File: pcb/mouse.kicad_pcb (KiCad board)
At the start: 2 copper layers, 70 x 45 mm, 74 parts, among them J1 USB_C_Receptacle_USB2.0, J2 Conn_01x05, J3 Conn_02x03_Counter_Clockwise, J4 Conn_01x06, J5 Conn_01x06, SW1 SW_Push_SPDT, SW2 SW_Push_SPDT, SW3 SW_Push_SPDT, SW4 SW_Push_SPDT, SW5 RotaryEncoder, SW6 SW_Push, U1 pmw3360-t2qu, U2 TLV70018_SOT23-5, U3 STM32F042K6Tx, U4 TLV70033_SOT23-5

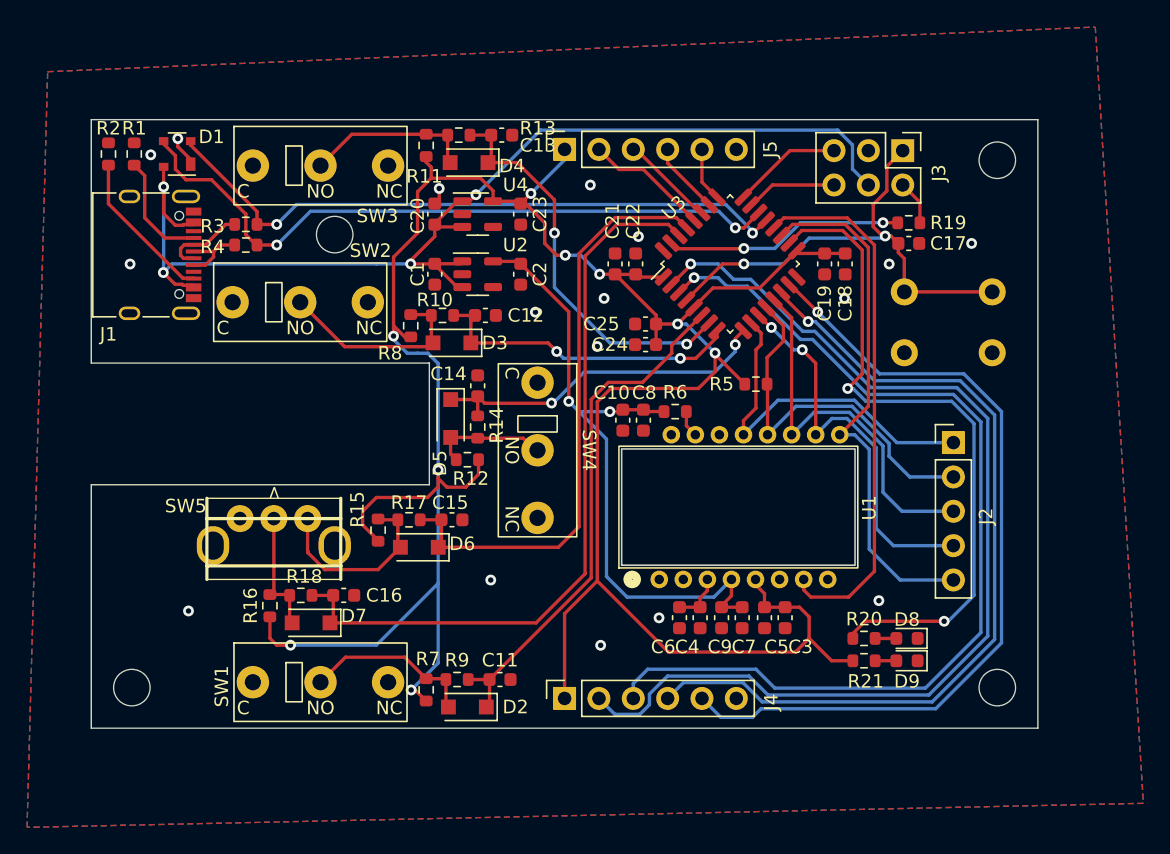
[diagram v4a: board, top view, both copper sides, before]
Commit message: added rounded corners to pcb
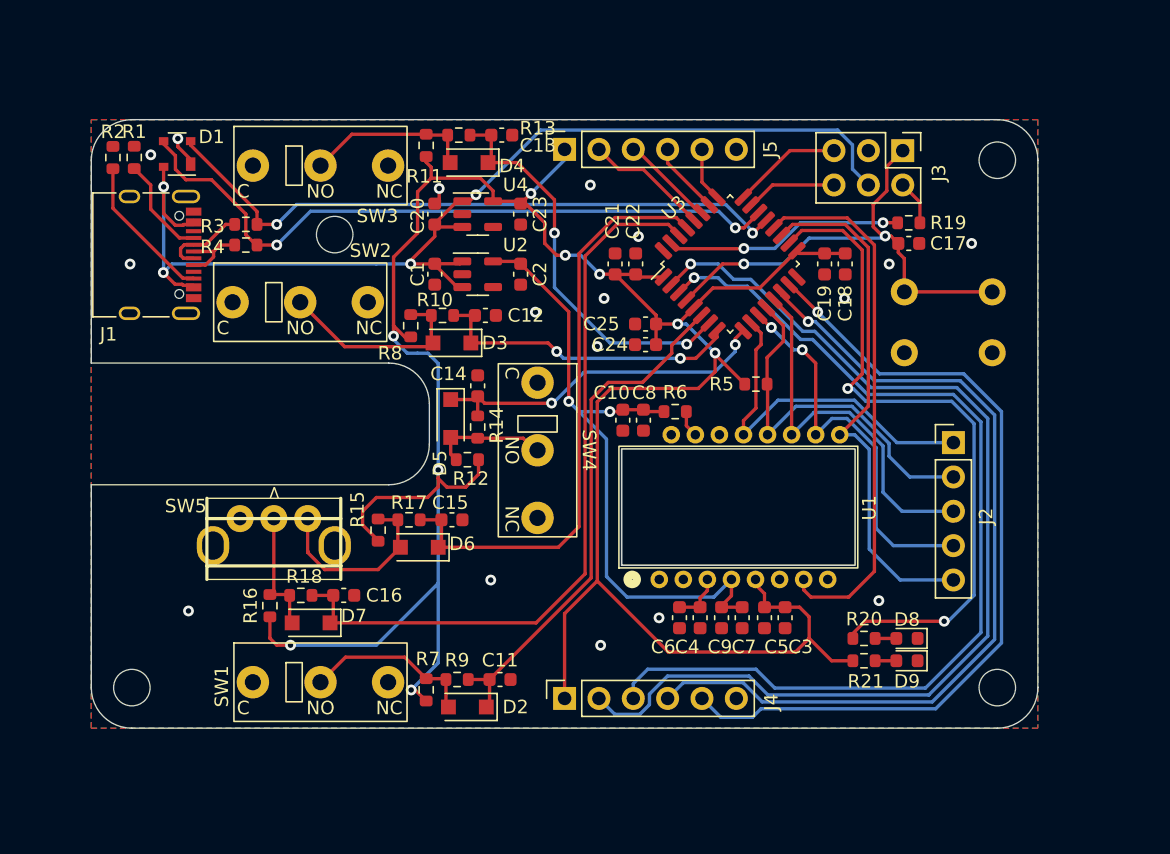
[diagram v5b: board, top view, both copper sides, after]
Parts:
- moved R2 0.42 mm to (101.6, 82.8)
- moved R1 0.25 mm to (103.2, 82.8)
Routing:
- net Net-(J1-PadA5): track 8.45 -> 7.57 mm
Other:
- outline, holes or cut-outs redrawn
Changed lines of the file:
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@@
   )
   (footprint "Resistor_SMD:R_0603_1608Metric" (layer "F.Cu")
-    (at 103.175 82.54 90)
+    (at 103.175 82.794 90)
     (descr "Resistor SMD 0603 (1608 Metric), square (rectangular) end terminal, IPC_7351 nominal, (Body size source: IPC-SM-782 page 72, https://www.pcb-3d.com/wordpress/wp-content/uploads/ipc-sm-782a_amendment_1_and_2.pdf), generated with kicad-footprint-generator")
     (tags "resistor")
@@
   )
   (footprint "Resistor_SMD:R_0603_1608Metric" (layer "F.Cu")
-    (at 101.27 82.54 90)
+    (at 101.6 82.804 90)
     (descr "Resistor SMD 0603 (1608 Metric), square (rectangular) end terminal, IPC_7351 nominal, (Body size source: IPC-SM-782 page 72, https://www.pcb-3d.com/wordpress/wp-content/uploads/ipc-sm-782a_amendment_1_and_2.pdf), generated with kicad-footprint-generator")
     (tags "resistor")
@@
     )
   )
-  (gr_line (start 125 107) (end 125 98) (layer "Edge.Cuts") (width 0.1))
-  (gr_line (start 170 80) (end 170 125) (layer "Edge.Cuts") (width 0.1))
-  (gr_line (start 100 107) (end 125 107) (layer "Edge.Cuts") (width 0.1))
-  (gr_line (start 100 80) (end 170 80) (layer "Edge.Cuts") (width 0.1))
-  (gr_line (start 100 80) (end 100 98) (layer "Edge.Cuts") (width 0.1))
-  (gr_line (start 125 98) (end 100 98) (layer "Edge.Cuts") (width 0.1))
-  (gr_line (start 100 107) (end 100 125) (layer "Edge.Cuts") (width 0.1))
-  (gr_line (start 170 125) (end 100 125) (layer "Edge.Cuts") (width 0.1))
+  (gr_line (start 125 104) (end 125 101) (layer "Edge.Cuts") (width 0.1))
+  (gr_arc (start 122 98) (mid 124.12132 98.87868) (end 125 101) (layer "Edge.Cuts") (width 0.1))
+  (gr_line (start 170 83) (end 170 122) (layer "Edge.Cuts") (width 0.1))
+  (gr_line (start 100 107) (end 122 107) (layer "Edge.Cuts") (width 0.1))
+  (gr_line (start 103 80) (end 167 80) (layer "Edge.Cuts") (width 0.1))
+  (gr_line (start 100 83) (end 100 98) (layer "Edge.Cuts") (width 0.1))
+  (gr_arc (start 170 122) (mid 169.12132 124.12132) (end 167 125) (layer "Edge.Cuts") (width 0.1))
+  (gr_arc (start 100 83) (mid 100.87868 80.87868) (end 103 80) (layer "Edge.Cuts") (width 0.1))
+  (gr_arc (start 125 104) (mid 124.12132 106.12132) (end 122 107) (layer "Edge.Cuts") (width 0.1))
+  (gr_line (start 122 98) (end 100 98) (layer "Edge.Cuts") (width 0.1))
+  (gr_arc (start 167 80) (mid 169.12132 80.87868) (end 170 83) (layer "Edge.Cuts") (width 0.1))
+  (gr_line (start 100 107) (end 100 122) (layer "Edge.Cuts") (width 0.1))
+  (gr_line (start 167 125) (end 103 125) (layer "Edge.Cuts") (width 0.1))
+  (gr_arc (start 103 125) (mid 100.87868 124.12132) (end 100 122) (layer "Edge.Cuts") (width 0.1))
   (segment (start 125.575 87.935) (end 125.4 87.76) (width 0.25) (layer "F.Cu") (net 1))
   (segment (start 105.35 84.969) (end 105.35 86.944273) (width 0.25) (layer "F.Cu") (net 1))
@@
   (segment (start 157.96875 118.364) (end 159.53125 118.364) (width 0.25) (layer "F.Cu") (net 21))
   (segment (start 157.96875 120.015) (end 159.53125 120.015) (width 0.25) (layer "F.Cu") (net 22))
-  (segment (start 105.448 88.75) (end 107.57 88.75) (width 0.25) (layer "F.Cu") (net 23))
-  (segment (start 103.175 83.365) (end 103.94952 84.13952) (width 0.25) (layer "F.Cu") (net 23))
-  (segment (start 103.94952 87.25152) (end 105.448 88.75) (width 0.25) (layer "F.Cu") (net 23))
-  (segment (start 103.94952 84.13952) (end 103.94952 87.25152) (width 0.25) (layer "F.Cu") (net 23))
+  (segment (start 104.394 84.838) (end 103.175 83.619) (width 0.25) (layer "F.Cu") (net 23))
+  (segment (start 107.57 88.75) (end 106.520009 88.75) (width 0.25) (layer "F.Cu") (net 23))
+  (segment (start 104.394 86.623991) (end 104.394 84.838) (width 0.25) (layer "F.Cu") (net 23))
+  (segment (start 106.520009 88.75) (end 104.394 86.623991) (width 0.25) (layer "F.Cu") (net 23))
   (segment (start 107.57 90.75) (end 108.444022 90.75) (width 0.25) (layer "F.Cu") (net 24))
   (segment (start 107.57 89.75) (end 109.046 89.75) (width 0.25) (layer "F.Cu") (net 24))
@@
   (segment (start 107.57 90.25) (end 106.821 90.25) (width 0.25) (layer "F.Cu") (net 25))
   (segment (start 106.821 90.25) (end 106.604 90.033) (width 0.25) (layer "F.Cu") (net 25))
-  (segment (start 107.544511 91.724511) (end 106.771511 91.724511) (width 0.25) (layer "F.Cu") (net 27))
-  (segment (start 106.771511 91.724511) (end 101.27 86.223) (width 0.25) (layer "F.Cu") (net 27))
-  (segment (start 101.27 86.223) (end 101.27 83.365) (width 0.25) (layer "F.Cu") (net 27))
-  (segment (start 107.57 91.75) (end 107.544511 91.724511) (width 0.25) (layer "F.Cu") (net 27))
+  (segment (start 101.6 86.552984) (end 106.771527 91.724511) (width 0.25) (layer "F.Cu") (net 27))
+  (segment (start 106.771527 91.724511) (end 107.544511 91.724511) (width 0.25) (layer "F.Cu") (net 27))
+  (segment (start 107.544511 91.724511) (end 107.57 91.75) (width 0.25) (layer "F.Cu") (net 27))
+  (segment (start 101.6 83.629) (end 101.6 86.552984) (width 0.25) (layer "F.Cu") (net 27))
   (segment (start 149.149 97.018) (end 149.53 96.637) (width 0.25) (layer "F.Cu") (net 29))
   (segment (start 149.53 95.782427) (end 148.781957 95.034384) (width 0.25) (layer "F.Cu") (net 29))
@@
     (polygon
       (pts
-        (xy 177.8 130.556)
-        (xy 95.25 132.334)
-        (xy 96.774 76.454)
-        (xy 174.244 73.152)
+        (xy 170 125)
+        (xy 100 125)
+        (xy 100 80)
+        (xy 170 80)
       )
     )

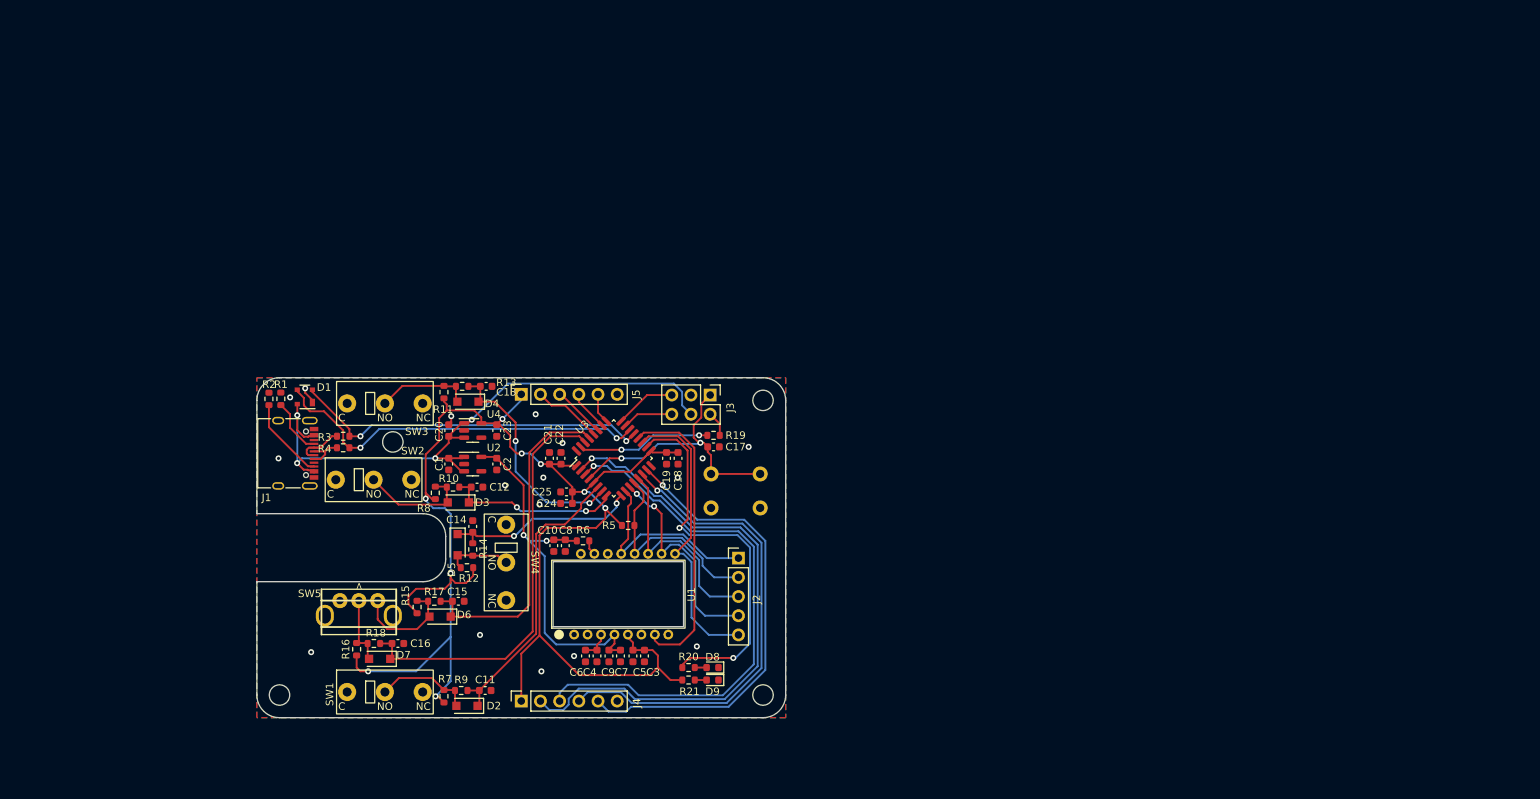
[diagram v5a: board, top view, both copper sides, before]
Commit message: manually connected GND on pcb
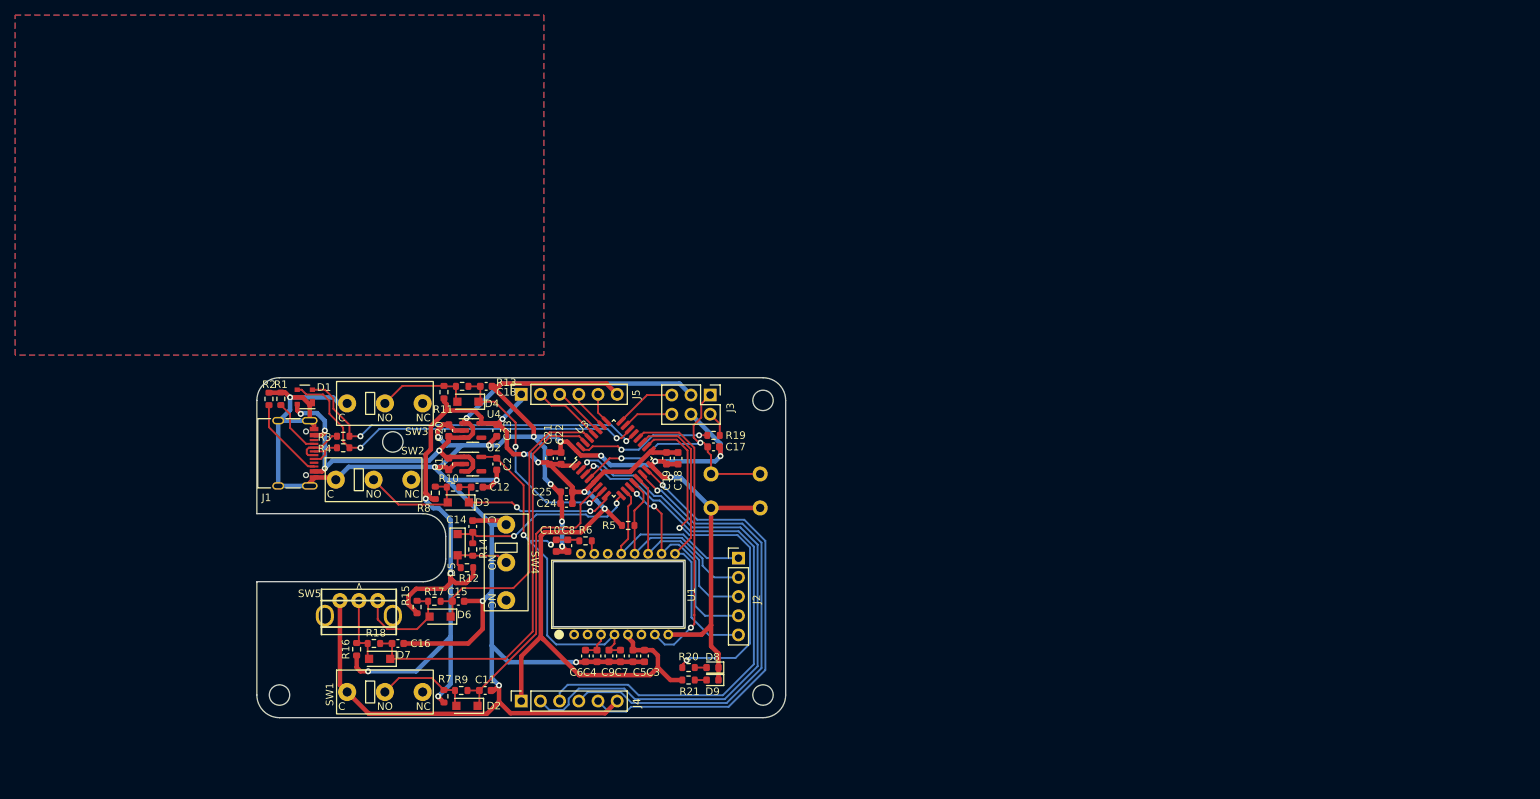
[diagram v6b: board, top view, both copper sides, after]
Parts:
- moved C10 0.33 mm to (139.6, 102.2)
- moved C8 0.33 mm to (141.2, 102.2)
- moved R6 0.33 mm to (143.5, 101.6)
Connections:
- J3 pad 3: GND -> +5V
- J3 pad 4: +5V -> GND
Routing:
- net GND: track 3.54 -> 363.6 mm
- net +5V: track 84.4 -> 79.6 mm, vias 4 -> 5
- net /buttons/ZA: track 44.3 -> 40.9 mm
- net +3V3: track 198.3 -> 196.3 mm
- net /buttons/LEFT: track 38.6 -> 39.7 mm
- net /mcu/USB_DM: track 47.8 -> 48.8 mm
- net /mcu/SENSOR_RESET: track 39.7 -> 38.8 mm, vias 0 -> 1
- net +1V8: track 48.6 -> 49.3 mm

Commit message: connected long loose ends of pcb traces, repoured copper pours
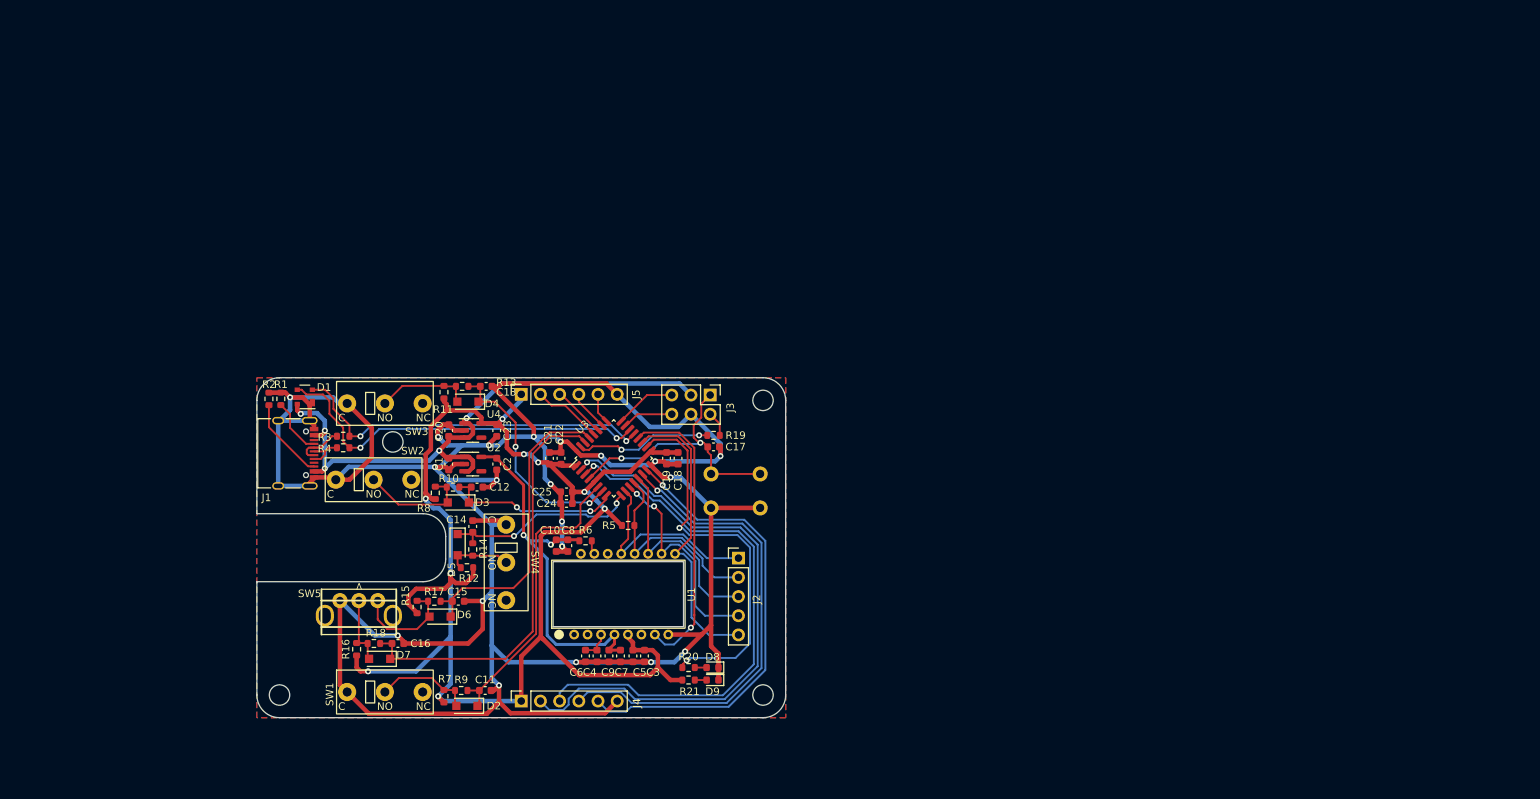
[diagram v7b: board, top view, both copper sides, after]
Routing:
- net GND: track 363.6 -> 420.4 mm, vias 17 -> 20
- net +3V3: track 196.3 -> 207.5 mm

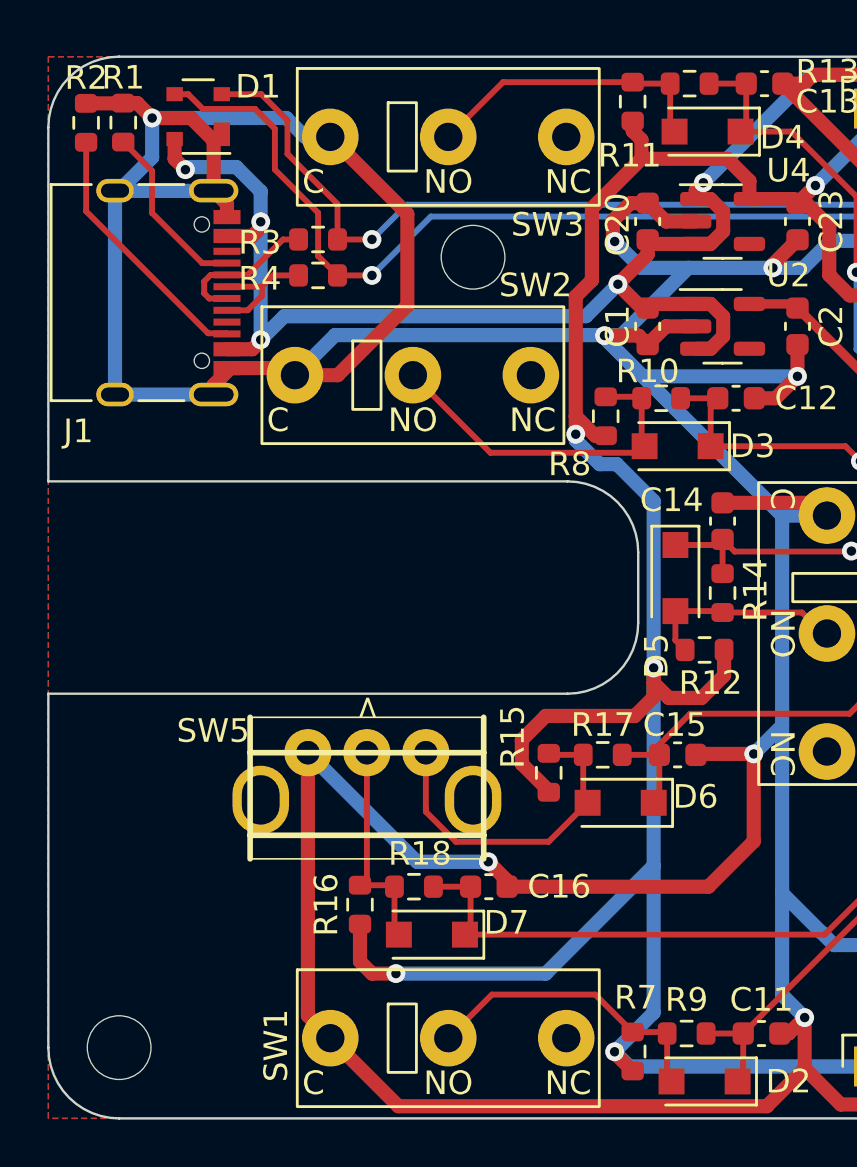
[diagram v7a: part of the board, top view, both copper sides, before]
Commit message: updated encoder position and widened wheel gap
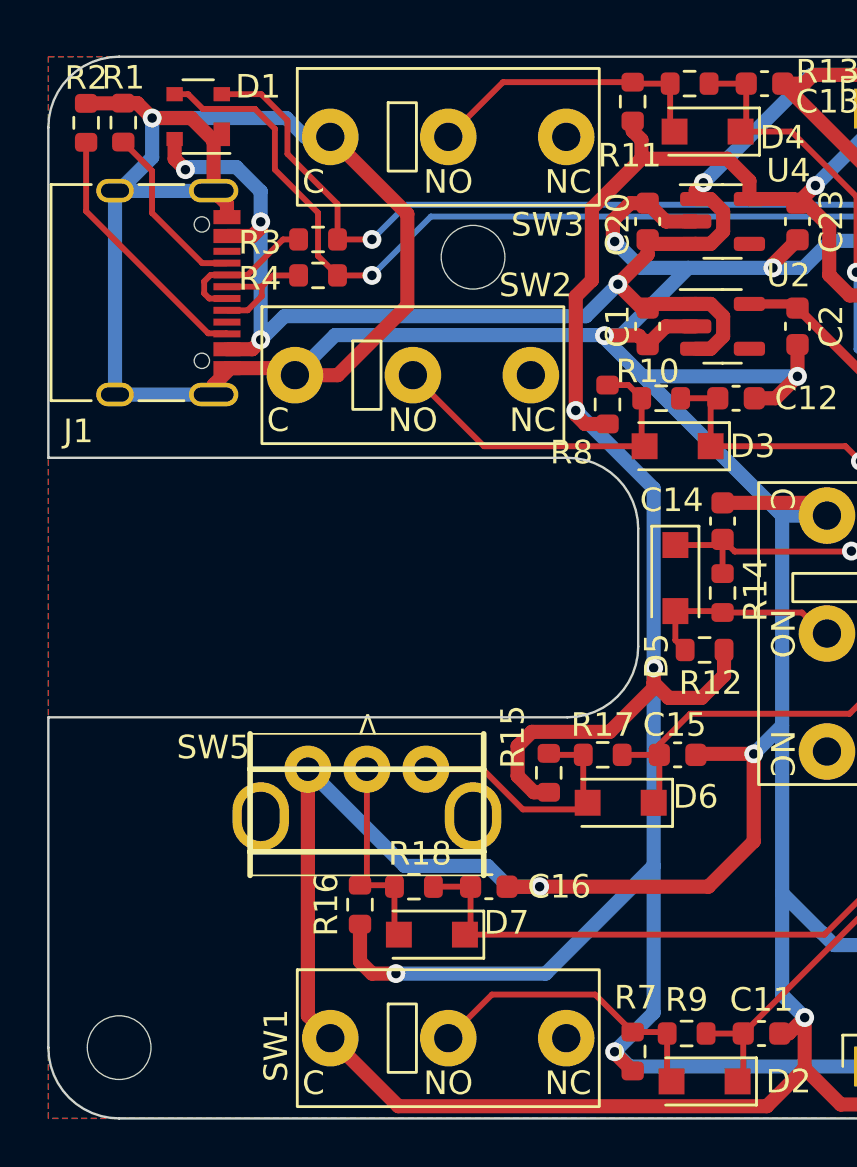
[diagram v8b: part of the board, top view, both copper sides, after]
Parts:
- moved SW5 0.70 mm to (113.5, 110.2)
- moved R8 0.50 mm to (123.7, 94.7)
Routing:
- net Net-(D6-Pad2): track 14.2 -> 11.3 mm
- net Net-(D7-Pad2): track 9.33 -> 8.63 mm
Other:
- outline, holes or cut-outs redrawn
